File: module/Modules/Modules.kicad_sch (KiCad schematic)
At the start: 13 parts, among them J1 Conn_01x04_MountingPin, J2 Conn_01x04, J3 Conn_01x04, J4 Conn_01x04, U1 COM-09032, U2 LTC4316xDD, U3 24LC32, U7 24AA02-OT, U9 ADS1115IDGS

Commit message: update
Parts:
- added JP1: WP, Jumper:SolderJumper-2_P1.3mm_Open_RoundedPad1.0x1.5mm, symbol Jumper:SolderJumper_2_Open
- added JP2: int, Jumper:SolderJumper-2_P1.3mm_Open_RoundedPad1.0x1.5mm, symbol Jumper:SolderJumper_2_Open
- U2: now not fitted; now left out of the parts list
- U3: now left out of the parts list
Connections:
- net Gnd: now also R1.1, R3.1, U7.2 (V_{SS}); no longer R1.2, R3.2, U3.4 (GND)
- net I03: no longer U3.3 (A2)
- net IO1: no longer U3.1 (A0)
- net IO2: no longer U3.2 (A1)
- net SCL: now also U7.1 (SCL); no longer U3.6 (SCL)
- net SDA: now also U7.3 (SDA); no longer U3.5 (SDA)
- net Vdd: now also U7.4 (V_{CC}), JP1.2 (B), JP2.2 (B); no longer U3.8 (VCC)
- net int: now also R1.2, JP2.1 (A)
- net wp: now also R3.2, U7.5 (WP), JP1.1 (A); no longer U3.7 (WP)
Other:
- moved on the sheet: R1, R3, U3, U7

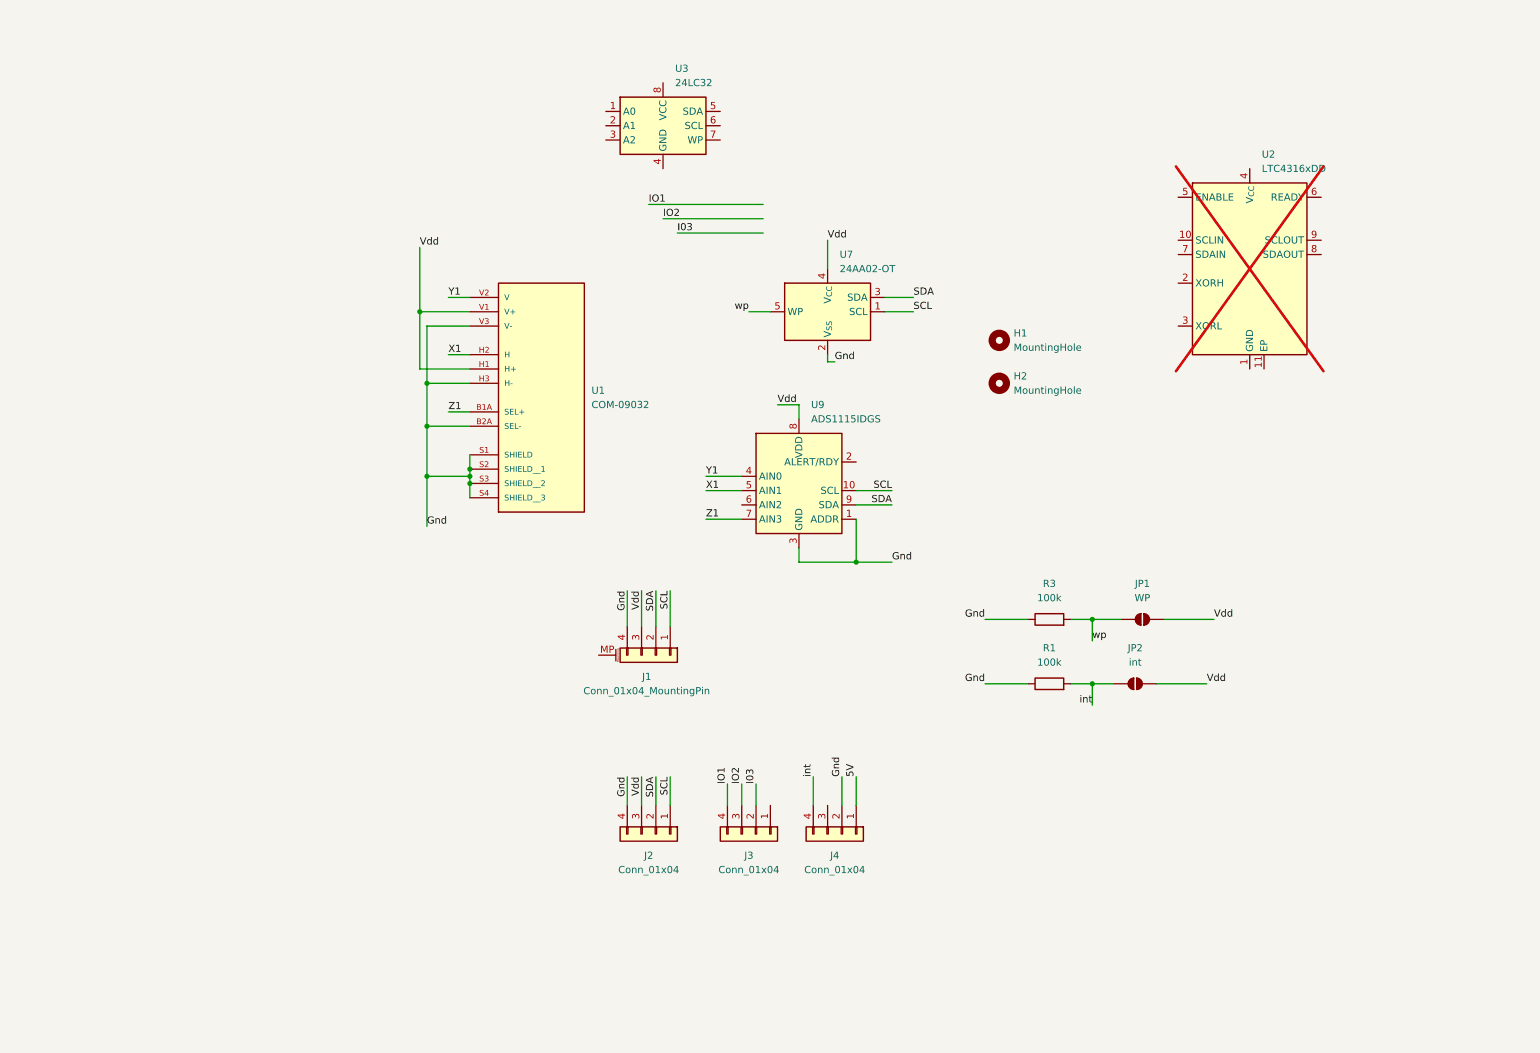
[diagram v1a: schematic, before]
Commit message: module spec update
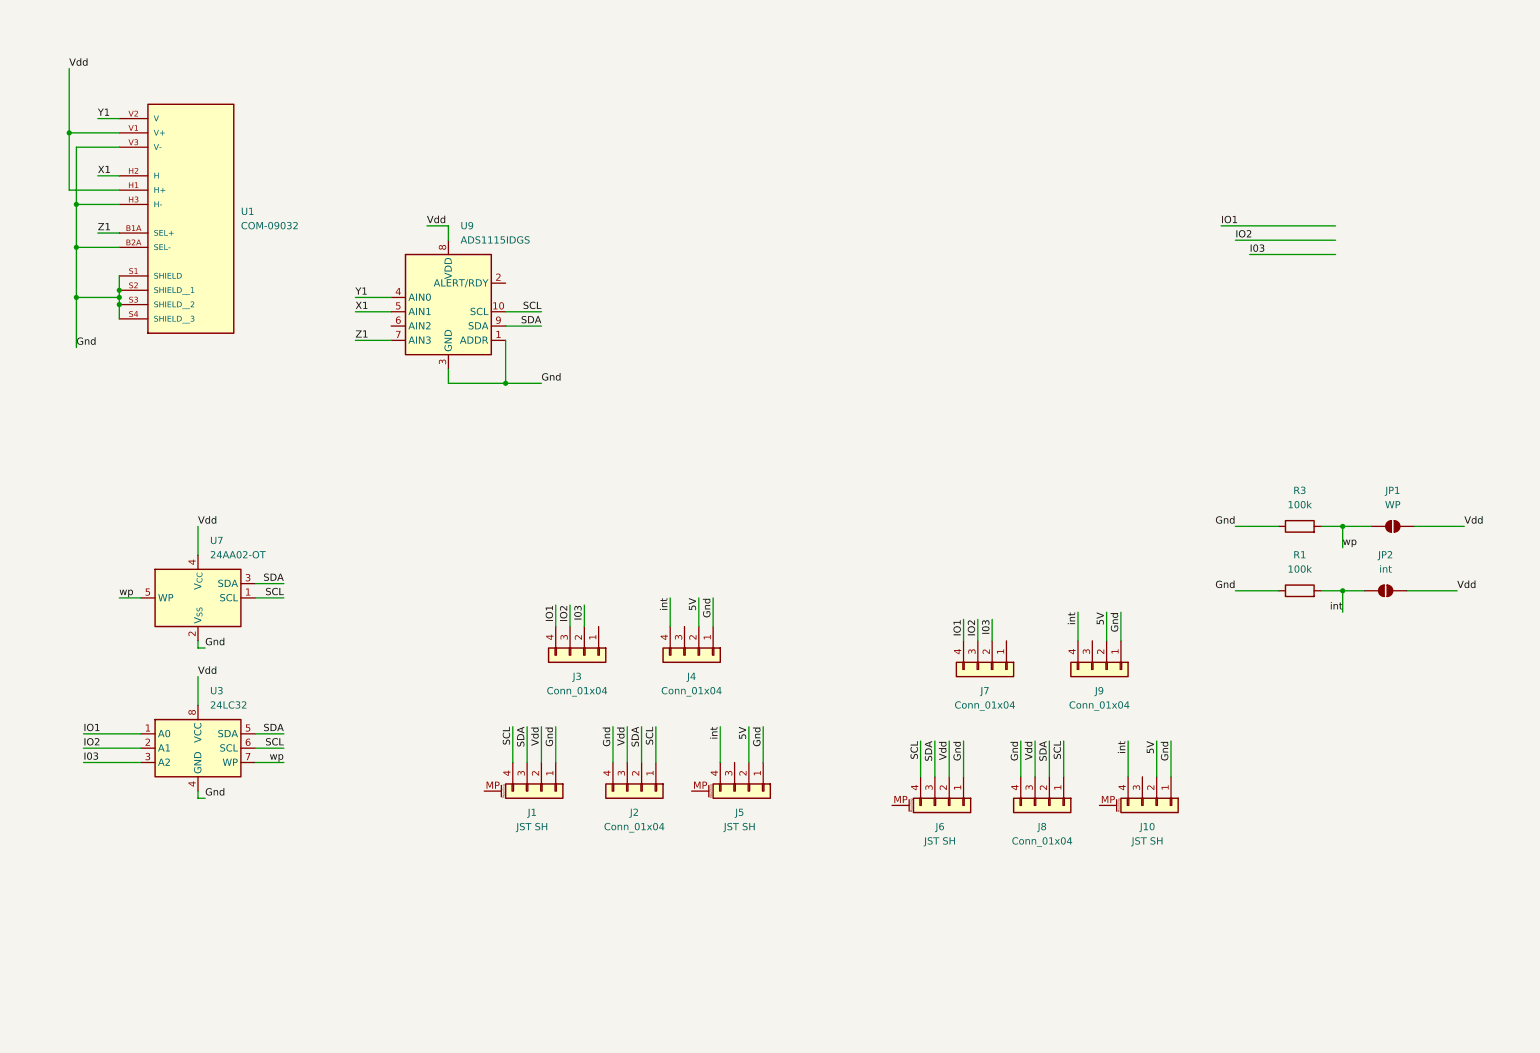
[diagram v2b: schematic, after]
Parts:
- removed H1, H2: MountingHole, MountingHole:MountingHole_2.2mm_M2, symbol Mechanical:MountingHole
- removed U2: LTC4316xDD, Package_SO:MSOP-10_3x3mm_P0.5mm, symbol Interface_Expansion:LTC4316xDD
- added J10, J5, J6: JST SH, Connector_JST:JST_SH_SM04B-SRSS-TB_1x04-1MP_P1.00mm_Horizontal, symbol Connector_Generic_MountingPin:Conn_01x04_MountingPin
- added J7, J8, J9: Conn_01x04, Connector_PinSocket_2.54mm:PinSocket_1x04_P2.54mm_Vertical, symbol Connector_Generic:Conn_01x04
- J1: value Conn_01x04_MountingPin -> JST SH; footprint Connector_JST:JST_SH_BM04B-SRSS-TB_1x04-1MP_P1.00mm_Vertical -> Connector_JST:JST_SH_SM04B-SRSS-TB_1x04-1MP_P1.00mm_Horizontal
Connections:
- net 5V: now also J4.2 (Pin_2), J10.2 (Pin_2), J5.2 (Pin_2), J9.2 (Pin_2); no longer J4.1 (Pin_1)
- net Gnd: now also J1.1 (Pin_1), J4.1 (Pin_1), U3.4 (GND), J10.1 (Pin_1), J5.1 (Pin_1), J6.1 (Pin_1), J8.4 (Pin_4), J9.1 (Pin_1); no longer J1.4 (Pin_4), J4.2 (Pin_2)
- net I03: now also U3.3 (A2), J7.2 (Pin_2)
- net IO1: now also U3.1 (A0), J7.4 (Pin_4)
- net IO2: now also U3.2 (A1), J7.3 (Pin_3)
- net SCL: now also J1.4 (Pin_4), U3.6 (SCL), J6.4 (Pin_4), J8.1 (Pin_1); no longer J1.1 (Pin_1)
- net SDA: now also J1.3 (Pin_3), U3.5 (SDA), J6.3 (Pin_3), J8.2 (Pin_2); no longer J1.2 (Pin_2)
- net Vdd: now also J1.2 (Pin_2), U3.8 (VCC), J6.2 (Pin_2), J8.3 (Pin_3); no longer J1.3 (Pin_3)
- net int: now also J10.4 (Pin_4), J5.4 (Pin_4), J9.4 (Pin_4)
- net wp: now also U3.7 (WP)
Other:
- moved on the sheet: J1, J2, J3, J4, JP1, JP2, R1, R3, U1, U3, U7, U9

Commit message: updated templet and renamed lib files
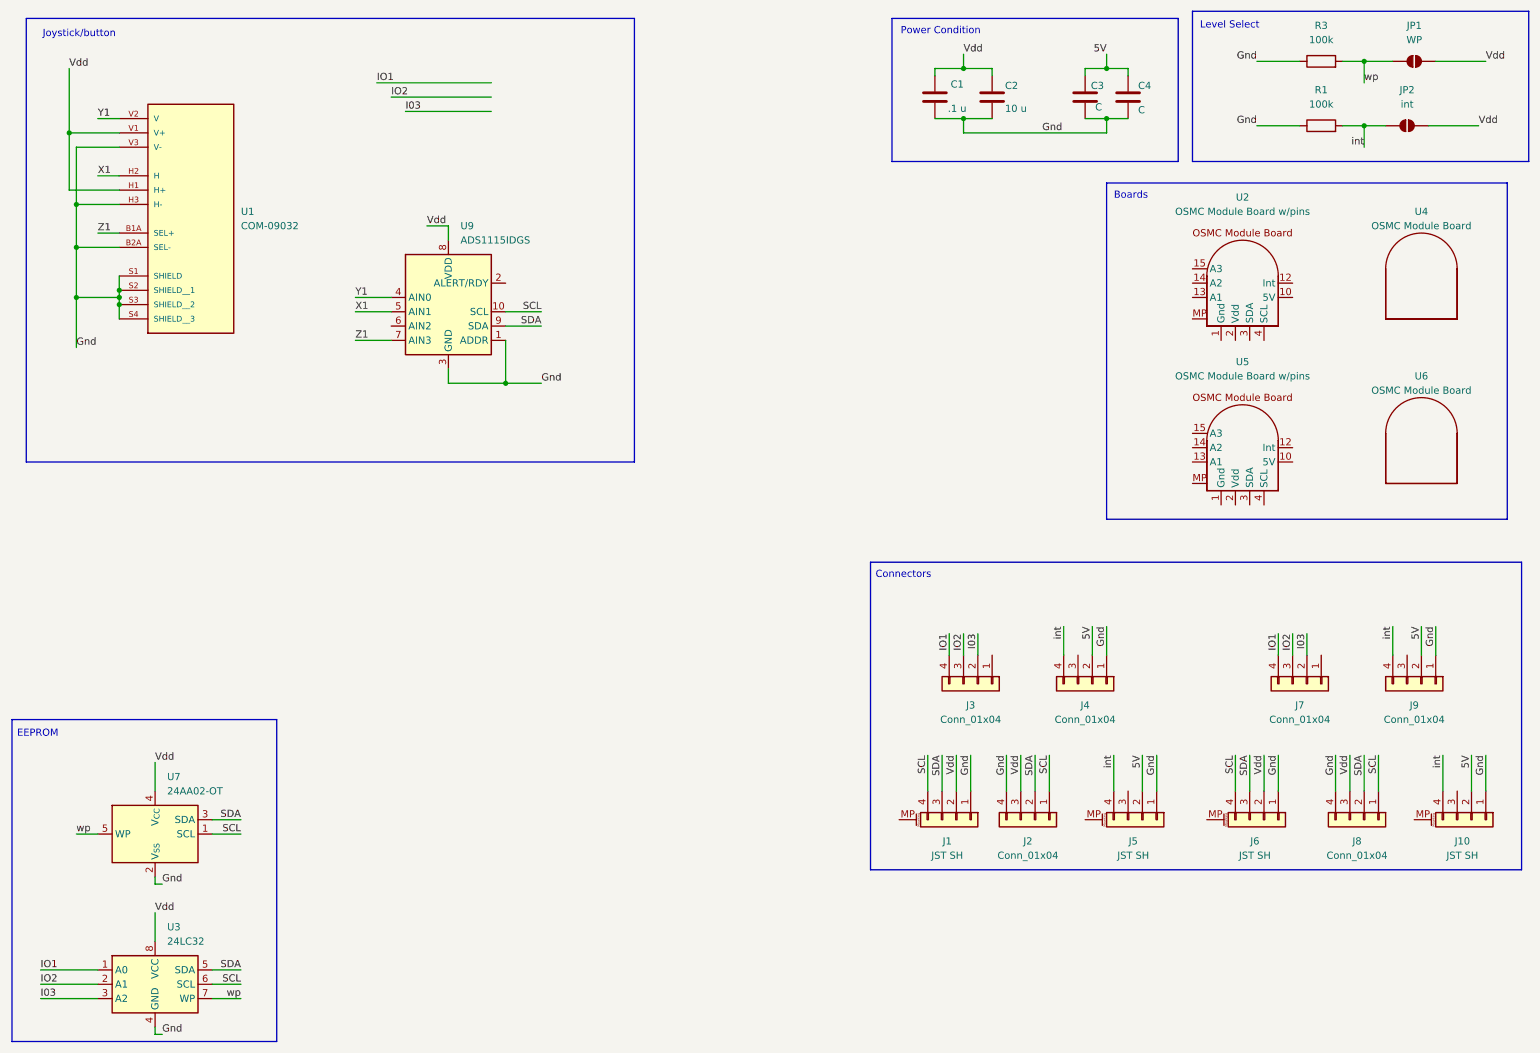
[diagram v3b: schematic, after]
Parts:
- added C1: .1 u, Capacitor_SMD:C_0603_1608Metric_Pad1.08x0.95mm_HandSolder, symbol Device:C
- added C2: 10 u, Capacitor_SMD:C_0603_1608Metric_Pad1.08x0.95mm_HandSolder, symbol Device:C
- added C3, C4: C, Capacitor_SMD:C_0603_1608Metric_Pad1.08x0.95mm_HandSolder, symbol Device:C
- added U2: OSMC Module Board w/pins, OSMC_Module:Module standard pin, symbol OSMC_Module:Input_Module
- added U4: OSMC Module Board, OSMC_Module:Module standard v2, symbol OSMC_Module:Input_Module_Pinless
- added U5: OSMC Module Board w/pins, OSMC_Module:Module standard pin v2, symbol OSMC_Module:Input_Module
- added U6: OSMC Module Board, OSMC_Module:Module standard, symbol OSMC_Module:Input_Module_Pinless
- U7: footprint Package_TO_SOT_SMD:SOT-23-5 -> Package_TO_SOT_SMD:SOT-23-5_HandSoldering
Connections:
- net 5V: now also C3.1, C4.1
- net Gnd: now also C1.2, C2.2, C3.2, C4.2
- net Vdd: now also C1.1, C2.1
- new net: U2.1 (Gnd), U2.5 (Gnd), U2.9 (Gnd)
- new net: U2.10 (5V), U2.16 (NC)
- new net: U2.2 (Vdd), U2.6 (Vdd)
- new net: U2.3 (SDA), U2.7 (SDA)
- new net: U2.4 (SCL), U2.8 (SCL)
- new net: U5.1 (Gnd), U5.5 (Gnd), U5.9 (Gnd)
- new net: U5.10 (5V), U5.16 (NC)
- new net: U5.2 (Vdd), U5.6 (Vdd)
- new net: U5.3 (SDA), U5.7 (SDA)
- new net: U5.4 (SCL), U5.8 (SCL)
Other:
- note added: "Boards"
- note added: "Connectors"
- note added: "EEPROM"
- note added: "Joystick/button"
- note added: "Level Select"
- note added: "Power Condition"
- moved on the sheet: J1, J10, J2, J3, J4, J5, J6, J7, J8, J9, JP1, JP2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

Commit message: update
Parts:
- C2: value 10 u -> .1 u
- U2: footprint OSMC_Module:Module standard pin -> OSMC_Module:Module standard pin small
- U4: footprint OSMC_Module:Module standard v2 -> OSMC_Module:Module standard small
- U5: footprint OSMC_Module:Module standard pin v2 -> OSMC_Module:Module standard pin large
- U6: footprint OSMC_Module:Module standard -> OSMC_Module:Module standard large
- U7: footprint Package_TO_SOT_SMD:SOT-23-5_HandSoldering -> Package_TO_SOT_SMD:SOT-23-5
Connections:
- net at U2.1 (Gnd), U2.5 (Gnd), U2.9 (Gnd): now also U2.16 (GND)
- net at U2.10 (5V): now also U2.15 (5V)
- net at U2.12 (Int): now also U2.13 (Int)
- net at U2.14 (OPT): now also U2.11 (OPT)
- net at U5.1 (Gnd), U5.5 (Gnd), U5.9 (Gnd): now also U5.16 (GND)
- net at U5.10 (5V): now also U5.15 (5V)
- net at U5.12 (Int): now also U5.13 (Int)
- net at U5.14 (OPT): now also U5.11 (OPT)
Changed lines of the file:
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@@
 			)
 		)
-		(property "Value" "10 u"
+		(property "Value" ".1 u"
 			(at 190.246 29.972 0)
 			(effects
@@
 			)
 		)
-		(property "Footprint" "OSMC_Module:Module standard pin"
+		(property "Footprint" "OSMC_Module:Module standard pin small"
 			(at 232.41 54.61 0)
 			(effects
@@
 		(pin "15"
 		)
-		(pin "10"
+		(pin "20"
 		)
 		(pin "7"
@@
 		)
 		(pin "4"
+		)
+		(pin "19"
+		)
+		(pin "18"
+		)
+		(pin "17"
+		)
+		(pin "11"
 		)
 		(instances
@@
 	)
 	(symbol
-		(lib_name "Input_Module_1")
 		(lib_id "OSMC_Module:Input_Module")
 		(at 232.41 83.82 0)
@@
 			)
 		)
-		(property "Footprint" "OSMC_Module:Module standard pin v2"
+		(property "Footprint" "OSMC_Module:Module standard pin large"
 			(at 232.41 83.82 0)
 			(effects
@@
 		(pin "15"
 		)
-		(pin "10"
+		(pin "18"
 		)
 		(pin "7"
@@
 		)
 		(pin "4"
+		)
+		(pin "19"
+		)
+		(pin "20"
+		)
+		(pin "17"
+		)
+		(pin "11"
 		)
 		(instances
@@
 			)
 		)
-		(property "Footprint" "OSMC_Module:Module standard"
+		(property "Footprint" "OSMC_Module:Module standard large"
 			(at 264.16 82.55 0)
 			(effects
@@
 			)
 		)
-		(property "Footprint" "Package_TO_SOT_SMD:SOT-23-5_HandSoldering"
+		(property "Footprint" "Package_TO_SOT_SMD:SOT-23-5"
 			(at 39.37 158.75 0)
 			(effects
@@
 			)
 		)
-		(property "Footprint" "OSMC_Module:Module standard v2"
+		(property "Footprint" "OSMC_Module:Module standard small"
 			(at 264.16 53.34 0)
 			(effects

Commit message: update
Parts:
- added R10, R11, R12, R13, R14, R15, R16, R17, R18, R19, R20, R7, R8, R9: 10k, OSMC_partsModule standard large, symbol OSMC_parts:R
- added R2, R4, R5, R6: 100k, OSMC_partsSolderJumper-2_P1.3mm_Open_RoundedPad1.0x1.5mm, symbol OSMC_parts:R
- added U10: LTC4317, OSMC_partsR_0805_2012Metric_Pad1.15x1.40mm_HandSolder, symbol OSMC_parts:LTC4317
- added U11: XIAO-ESP32-S3-DIP, OSMC_partsXIAO-ESP32-S3-DIP, symbol OSMC_parts:XIAO-ESP32-S3-DIP
- added U8: PCF8574DWR, OSMC_partsDW16-L, symbol OSMC_parts:PCF8574T
- C1, C2, C3, C4: footprint Capacitor_SMD:C_0603_1608Metric_Pad1.08x0.95mm_HandSolder -> OSMC_partsC_0603_1608Metric_Pad1.08x0.95mm_HandSolder; symbol Device:C -> OSMC_parts:C
- J1, J10, J5, J6: footprint Connector_JST:JST_SH_SM04B-SRSS-TB_1x04-1MP_P1.00mm_Horizontal -> OSMC_partsXDCR_COM-09032; symbol Connector_Generic_MountingPin:Conn_01x04_MountingPin -> OSMC_parts:Conn_01x04_MountingPin
- J2, J3, J4, J7, J8, J9: footprint Connector_PinSocket_2.54mm:PinSocket_1x04_P2.54mm_Vertical -> OSMC_partsJST_SH_SM04B-SRSS-TB_1x04-1MP_P1.00mm_Horizontal; symbol Connector_Generic:Conn_01x04 -> OSMC_parts:Conn_01x04
- JP1: footprint Jumper:SolderJumper-2_P1.3mm_Open_RoundedPad1.0x1.5mm -> OSMC_partsPinSocket_1x04_P2.54mm_Vertical; symbol Jumper:SolderJumper_2_Open -> OSMC_parts:SolderJumper_2_Open
- JP2: value int -> Det; footprint Jumper:SolderJumper-2_P1.3mm_Open_RoundedPad1.0x1.5mm -> OSMC_partsSolderJumper-2_P1.3mm_Open_RoundedPad1.0x1.5mm; symbol Jumper:SolderJumper_2_Open -> OSMC_parts:SolderJumper_2_Open
- R1, R3: footprint PCM_Resistor_SMD_AKL:R_0805_2012Metric_Pad1.15x1.40mm_HandSolder -> OSMC_partsSolderJumper-2_P1.3mm_Open_RoundedPad1.0x1.5mm; symbol Device:R -> OSMC_parts:R
- U1: footprint COM_09032:XDCR_COM-09032 -> OSMC_partsModule standard pin large; symbol COM-09032:Joystick-09032 -> OSMC_parts:Joystick-09032
- U2: footprint OSMC_Module:Module standard pin small -> OSMC_partsModule standard pin small; symbol OSMC_Module:Input_Module -> OSMC_parts:Input_Module
- U3: footprint Package_SO:SOIC-8_3.9x4.9mm_P1.27mm -> OSMC_partsModule standard small; symbol Memory_EEPROM:24LC32 -> OSMC_parts:24LC32; now not fitted
- U4: footprint OSMC_Module:Module standard small -> OSMC_partsDFN-16-1EP_3x5mm_P0.5mm_EP1.66x4.4mm; symbol OSMC_Module:Input_Module_Pinless -> OSMC_parts:Input_Module_Pinless
- U5: footprint OSMC_Module:Module standard pin large -> OSMC_partsSOIC-8_3.9x4.9mm_P1.27mm; symbol OSMC_Module:Input_Module -> OSMC_parts:Input_Module
- U6: footprint OSMC_Module:Module standard large -> OSMC_partsTSSOP-10_3x3mm_P0.5mm; symbol OSMC_Module:Input_Module_Pinless -> OSMC_parts:Input_Module_Pinless
- U7: footprint Package_TO_SOT_SMD:SOT-23-5 -> OSMC_partsSOT-23-5; symbol Memory_EEPROM:24AA02-OT -> OSMC_parts:24AA02-OT
- U9: footprint Package_SO:TSSOP-10_3x3mm_P0.5mm -> OSMC_partsR_0805_2012Metric_Pad1.15x1.40mm_HandSolder; symbol Analog_ADC:ADS1115IDGS -> OSMC_parts:ADS1115IDGS
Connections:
- net I03 is gone; now on net Gnd: J3.2 (Pin_2), J7.2 (Pin_2), U3.3 (A2)
- net IO1 is gone; now on net Gnd: J3.4 (Pin_4), J7.4 (Pin_4), U3.1 (A0)
- net IO2 is gone; now on net Gnd: J3.3 (Pin_3), J7.3 (Pin_3), U3.2 (A1)
- net 5V: now also U11.14 (5V)
- net Gnd: now also U11.13 (GND), U8.1 (A0), U8.2 (A1), U8.3 (A2), U8.8 (GND)
- net SCL: now also R12.2, U10.15 (SCLIN), U11.6 (PA9_A5_D5_SCL), U8.14 (SCL)
- net SDA: now also R15.2, U10.12 (SDAIN), U11.5 (PA8_A4_D4_SDA), U8.15 (SDA)
- net Vdd: now also R12.1, R15.1, R19.1, R2.1, R20.1, R4.1, R5.1, R6.1, U11.12 (3V3), U8.16 (VDD)
- net int: now also U9.2 (ALERT/RDY), U8.13 (~{INT}); no longer J4.4 (Pin_4), J9.4 (Pin_4), JP2.1 (A), R1.2
- net Opt: now reaches J4.3 (Pin_3)
- net Opt: now also J9.3 (Pin_3)
- new net: R14.2, R16.1, U10.6 (XORL1)
- new net: R17.2, U10.2 (ENABLE2)
- new net: R11.2, R13.1, U10.5 (XORH1)
- new net: R18.2, U10.8 (ENABLE1)
- new net B0: R2.2, U8.4 (P0)
- new net B1: R4.2, U8.5 (P1)
- new net B2: R5.2, U8.6 (P2)
- new net B3: R6.2, U8.7 (P3)
- new net Det: J4.4 (Pin_4), J9.4 (Pin_4), JP2.1 (A), R1.2
- new net GND: R13.2, R16.2, U10.1 (GND), U10.17 (EP), U10.3 (XORH2), U10.4 (XORL2)
- new net INT: U11.11 (PA6_A10_D10_MOSI)
- new net P0: U10.10 (READY1)
- new net P1: U10.9 (READY2)
- new net SCL0: R7.2, R8.2, U10.13 (SDAOUT1), U10.14 (SCLOUT1)
- new net SCL1: R10.2, R20.2, R9.2, U10.11 (SDAOUT2), U10.16 (SCLOUT2), U11.9 (PA7_A8_D8_SCK)
- new net SDA1: R19.2, U11.10 (PA5_A9_D9_MISO)
- new net VDD: R10.1, R11.1, R14.1, R17.1, R18.1, R7.1, R8.1, R9.1, U10.7 (VCC)
- no-connect marks 0 -> 4
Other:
- note added: "Address Translator"
- note added: "Address pins"
- note added: "IO Expander"
- note added: "Joystick and ADC"
- note added: "MCU"
- note removed: "Joystick/button"
- moved on the sheet: C1, C2, C3, C4, J1, J10, J2, J3, J4, J5, J6, J7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
